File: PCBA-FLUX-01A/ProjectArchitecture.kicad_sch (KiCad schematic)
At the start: 0 parts

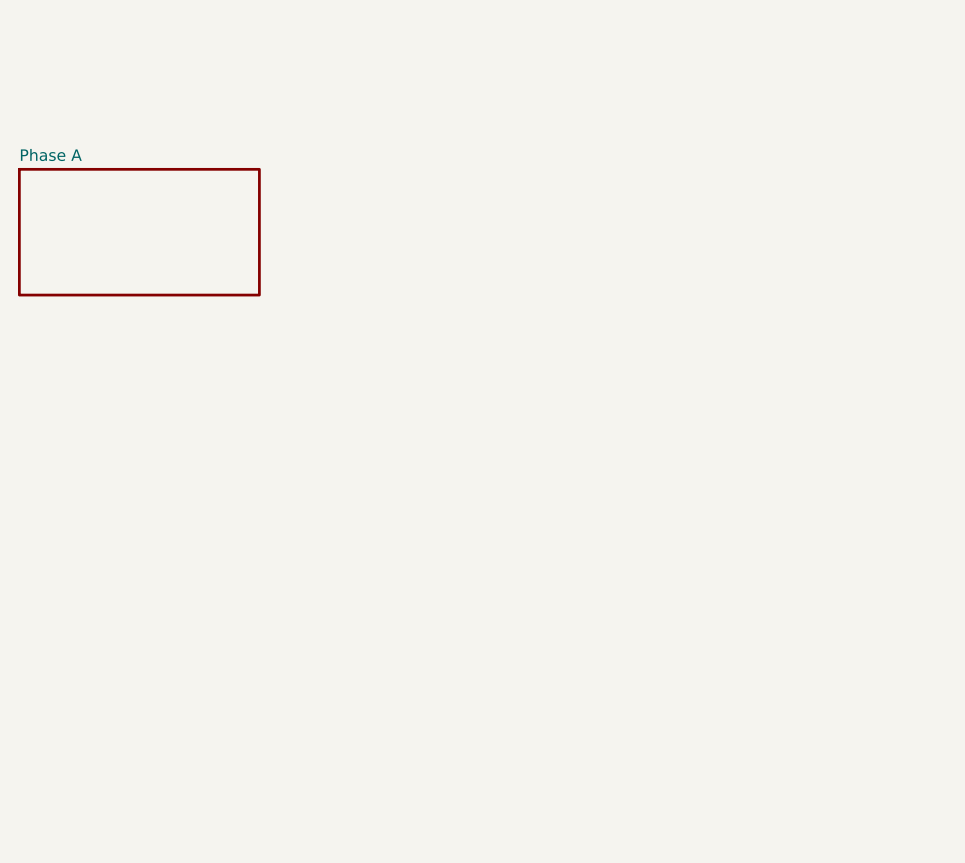
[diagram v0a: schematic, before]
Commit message: Finished inverter design and started working on MCU pin out
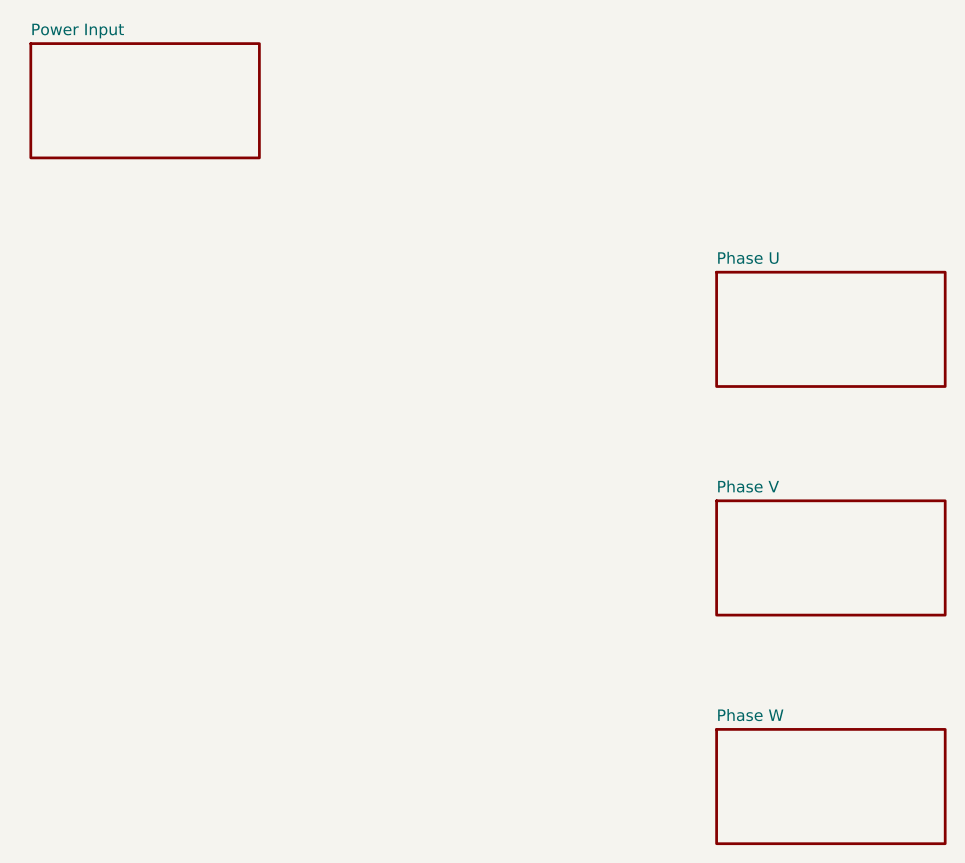
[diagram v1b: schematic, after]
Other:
- sheet Phase A renamed Phase U
- added sheet Phase V (PhaseV.kicad_sch)
- added sheet Phase W (PhaseW.kicad_sch)
- added sheet Power Input (Power Input.kicad_sch)
- sheet Phase U: file PhaseA.kicad_sch -> PhaseU.kicad_sch
- company: (none) -> Jovanovski Laboratory - JLAB
